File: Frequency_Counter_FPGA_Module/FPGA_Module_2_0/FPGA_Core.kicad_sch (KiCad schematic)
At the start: 97 parts, among them J1 Channel A, J2 Channel B, J3 CH A Test, J4 CH B Test, J5 GPS, J6 Input_board, J7 STM_mainboard, U1 MAX9601, U12 TLV9001IDCK, U2 MC100EP016A, U20 MC100EPT23DT, U24 MC100EPT23DT

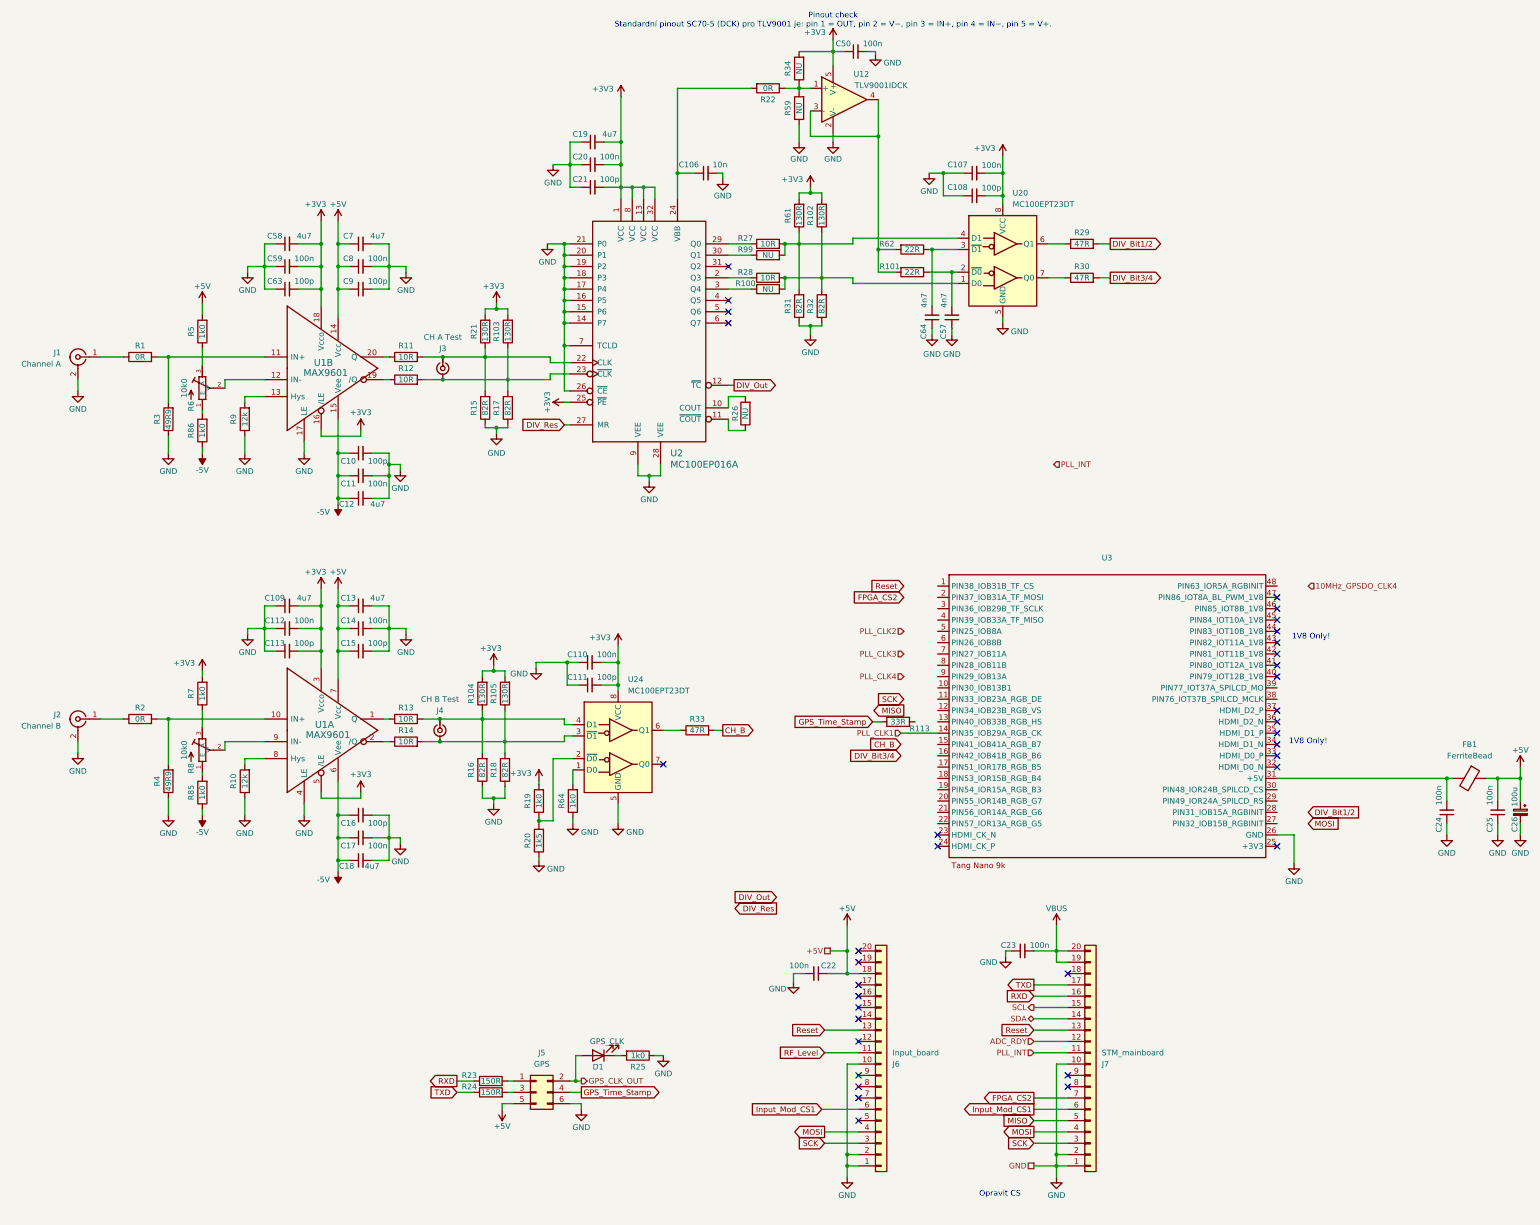
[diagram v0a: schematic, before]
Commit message: feat(boot): LED selftest blikaci kod + RTC LSE medium-low drive; UI 4.3" audit; FPGA HW revize
STM32H757 firmware:
- bootled.c/h: boot-time HW selftest diagnostika na LED_1 (PG3). Kazdy
  sledovany periferni init (FMC/SPI2/I2C4/DSIHOST/LTDC/USART1/RTC/ADC3/
  QUADSPI/I2C1) + display bring-up (panel probe/power-on/DSI start/
  TC358762) si zaznamena poradove cislo; pri zaseknuti v Error_Handler()
  LED bez displeje zabliká N-krat podle poradi. Regen-safe (jen chranene
  USER CODE hooky), bez zpozdeni v happy-path.
- RTC LSE Drive Capability LOW -> MEDIUM LOW (H757_LED.ioc): kompenzuje
  desky s predimenzovanymi zatezovymi kondenzatory krystalu (22pF misto
  18pF), ktere LSE nerozjizdely.
- UI audit pro realny 4,3" 800x480 panel (8,54 px/mm): hit-slop pilulek,
  fonty, HDR_PILL_LIMIT fit-check, Menu 3x4 mrizka s placeholdery, oprava
  ghost bugu AUTO CET/CEST tlacitka, sign-loss bug ve fmt_fixed/fmt_minmax.
  main-old layout zamrazen jako default (A/B srovnani, viz STATUS.md #14).

FPGA carrier v2.0 (KiCad): prubezne review checklisty a schema/PCB revize.

Co-Authored-By: OK2JNJ <ok2jnj@local>
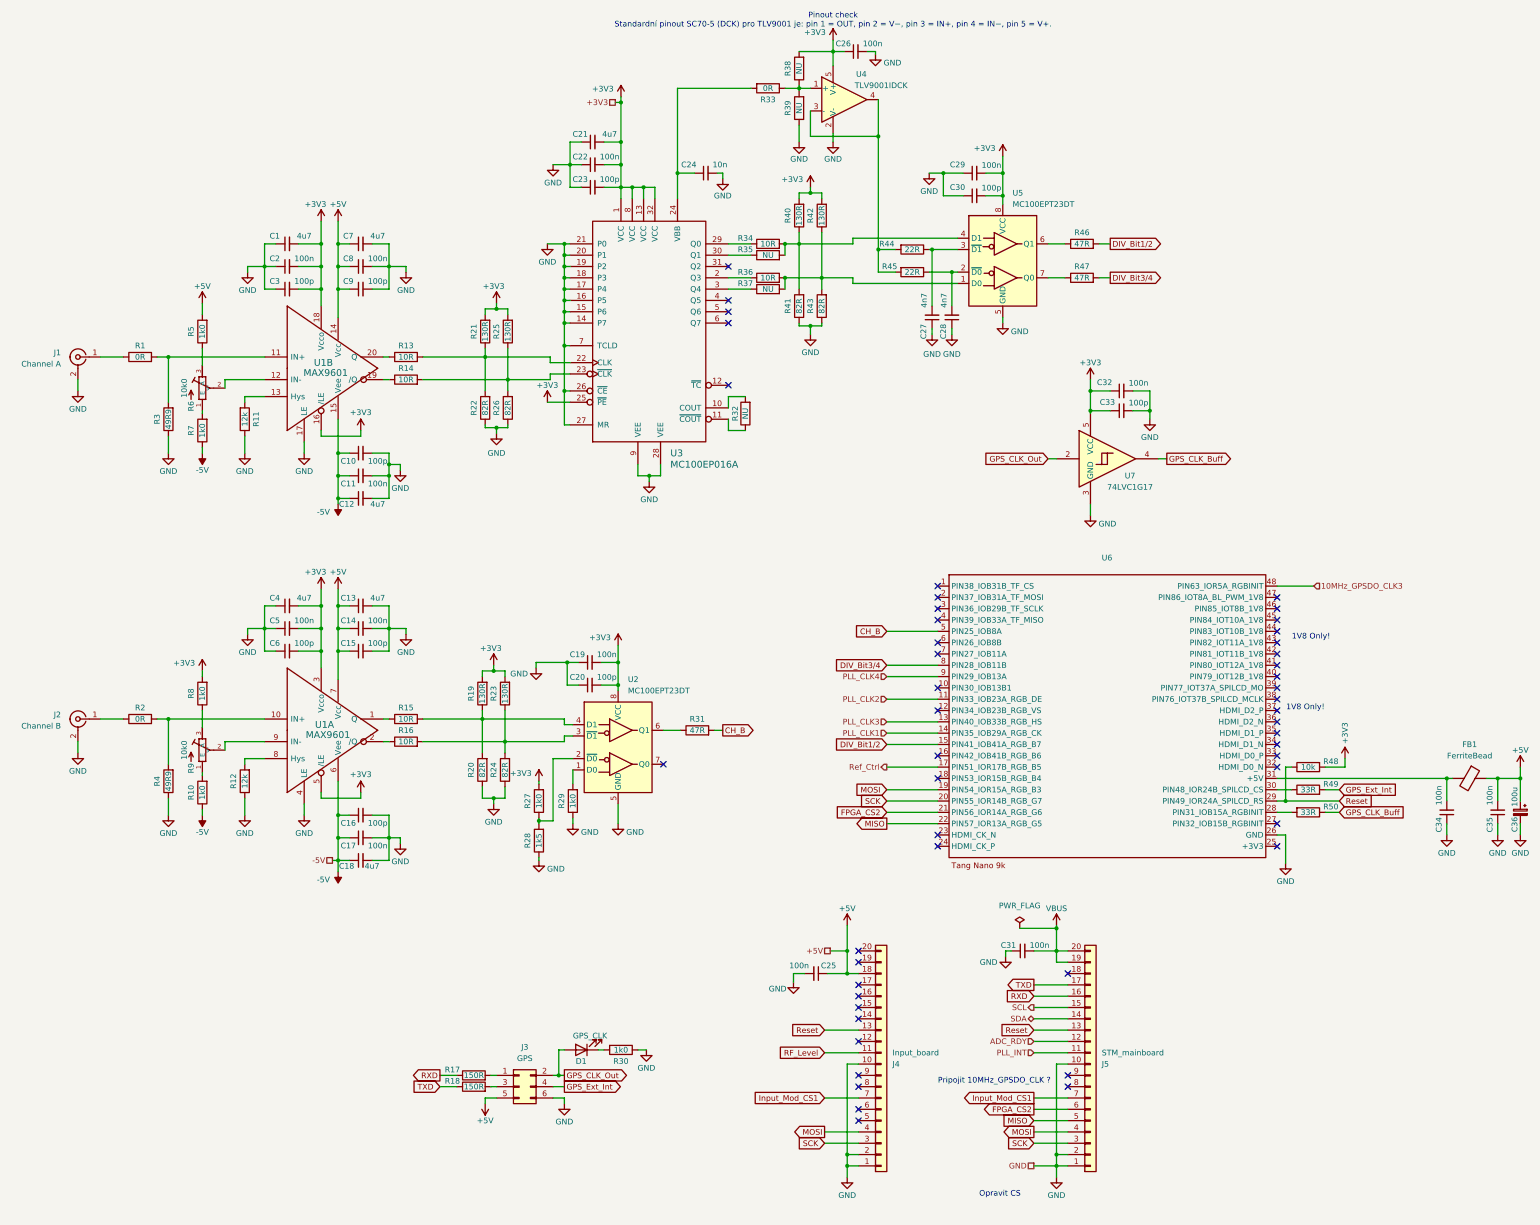
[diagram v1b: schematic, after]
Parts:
- removed J3: CH A Test, Connector_Coaxial:U.FL_Hirose_U.FL-R-SMT-1_Vertical, symbol Connector:Conn_Coaxial_Small
- removed J4: CH B Test, Connector_Coaxial:U.FL_Hirose_U.FL-R-SMT-1_Vertical, symbol Connector:Conn_Coaxial_Small
- removed U2: MC100EP016A, Package_QFP:LQFP-32_7x7mm_P0.8mm, symbol Counter_main-cache:MC100EP016A-RESCUE-Counter
- added C32: 100n, Capacitor_SMD:C_0805_2012Metric, symbol Device:C_Small
- added C33: 100p, Capacitor_SMD:C_0805_2012Metric, symbol Device:C_Small
- added R48: 10k, Resistor_SMD:R_0805_2012Metric, symbol Device:R
- added R50: 33R, Resistor_SMD:R_0805_2012Metric, symbol Device:R
- added U3: MC100EP016A, Package_QFP:LQFP-32_7x7mm_P0.8mm, symbol Counter_main-cache:MC100EP016A-RESCUE-Counter
- added U7: 74LVC1G17, Package_TO_SOT_SMD:SOT-23-5, symbol 74xGxx:74LVC1G17
- U6: renamed from U3; value ~ -> (none)
- renumbered C58 to C1, C110 to C19, C59 to C2, C111 to C20, C19 to C21, C20 to C22, C21 to C23, C106 to C24, C22 to C25, C50 to C26, C64 to C27, C57 to C28, C107 to C29, C63 to C3, C108 to C30, C23 to C31, C24 to C34, C25 to C35, C26 to C36, C109 to C4, C112 to C5, C113 to C6, J5 to J3, J6 to J4, J7 to J5, R85 to R10, R9 to R11, R10 to R12, R11 to R13, R12 to R14, R13 to R15, R14 to R16, R23 to R17, R24 to R18, R104 to R19, R16 to R20, R15 to R22, R105 to R23, R18 to R24, R103 to R25, R17 to R26, R19 to R27, R20 to R28, R64 to R29, R25 to R30, R33 to R31, R26 to R32, R22 to R33, R27 to R34, R99 to R35, R28 to R36, R100 to R37, R34 to R38, R59 to R39, R61 to R40, R31 to R41, R102 to R42, R32 to R43, R62 to R44, R101 to R45, R29 to R46, R30 to R47, R113 to R49, R86 to R7, R7 to R8, R8 to R9, U24 to U2, U12 to U4, U20 to U5
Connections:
- net +3V3: now also C32.1, C33.1, R48.2, U3.1 (VCC), U3.13 (VCC), U3.25 (~{PE}), U3.32 (VCC), U3.8 (VCC), U7.5 (VCC)
- net CH_B: now also U6.5 (PIN25_IOB8A)
- net DIV_Bit1/2: now also U6.15 (PIN41_IOB41A_RGB_B7)
- net DIV_Bit3/4: now also U6.8 (PIN28_IOB11B)
- net FPGA_CS2: now also J5.6 (Pin_6), U6.21 (PIN56_IOR14A_RGB_G6); no longer J5.7 (Pin_7)
- net GND: now also C32.2, C33.2, U3.14 (P7), U3.15 (P6), U3.16 (P5), U3.17 (P4), U3.18 (P3), U3.19 (P2), U3.20 (P1), U3.21 (P0), U3.26 (~{CE}), U3.27 (MR), U3.28 (VEE), U3.7 (TCLD), U3.9 (VEE), U7.3 (GND)
- net Input_Mod_CS1: now also J4.7 (Pin_7), J5.7 (Pin_7); no longer J4.6 (Pin_6), J5.6 (Pin_6)
- net MISO: now also U6.22 (PIN57_IOR13A_RGB_G5)
- net MOSI: now also U6.19 (PIN54_IOR15A_RGB_B3)
- net PLL_CLK2: now also U6.11 (PIN33_IOB23A_RGB_DE)
- net PLL_CLK3: now also U6.13 (PIN40_IOB33B_RGB_HS)
- net PLL_CLK4: now also U6.9 (PIN29_IOB13A)
- net Reset: now also U6.29 (PIN49_IOR24A_SPILCD_RS), R48.1
- net SCK: now also U6.20 (PIN55_IOR14B_RGB_G7)
- net at R37.1: now also U3.3 (Q4)
- net at R13.2, R21.1, R22.2: now also U3.22 (CLK)
- net at R14.2, R25.1, R26.2: now also U3.23 (~{CLK})
- net at C24.1, R33.2: now also U3.24 (VBB)
- net at R49.1: now also U6.30 (PIN48_IOR24B_SPILCD_CS)
- net at R36.1: now also U3.2 (Q3)
- net at R35.1: now also U3.30 (Q1)
- net at R32.1: now also U3.11 (~{COUT})
- net at R32.2: now also U3.10 (COUT)
- net at R34.1: now also U3.29 (Q0)
- net Ref_Ctrl: now reaches U6.17 (PIN51_IOR17B_RGB_B5)
- net at U6.28 (PIN31_IOB15A_RGBINIT): now also R50.2
- net 10MHz_GPSDO_CLK3: now reaches U6.48 (PIN63_IOR5A_RGBINIT)
- net GPS_CLK_OUT renamed GPS_CLK_Out
- net GPS_CLK_Out: now also U7.2
- net GPS_Time_Stamp renamed GPS_Ext_Int
- new net GPS_CLK_Buff: R50.1, U7.4
- no-connect marks 36 -> 50
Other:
- note added: "Pripojit 10MHz_GPSDO_CLK ?"
- moved on the sheet: D1, J3, R11, R17, R18, R30, R49

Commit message: feat(hw): FPGA carrier v2.0 — aktualizace schematu + PCB + checklist
KiCad FPGA_Module_2_0 (FPGA_Core/GPSDO/I2C_devices/power_supply schemata,
PCB layout, project), BOARD_V20_CHECKLIST.md. Odstranen zastaraly
FPGA_module_schematic.pdf (nahrazen exportem FPGA_module.pdf).

Co-Authored-By: OK2JNJ <ok2jnj@users.noreply.github.com>
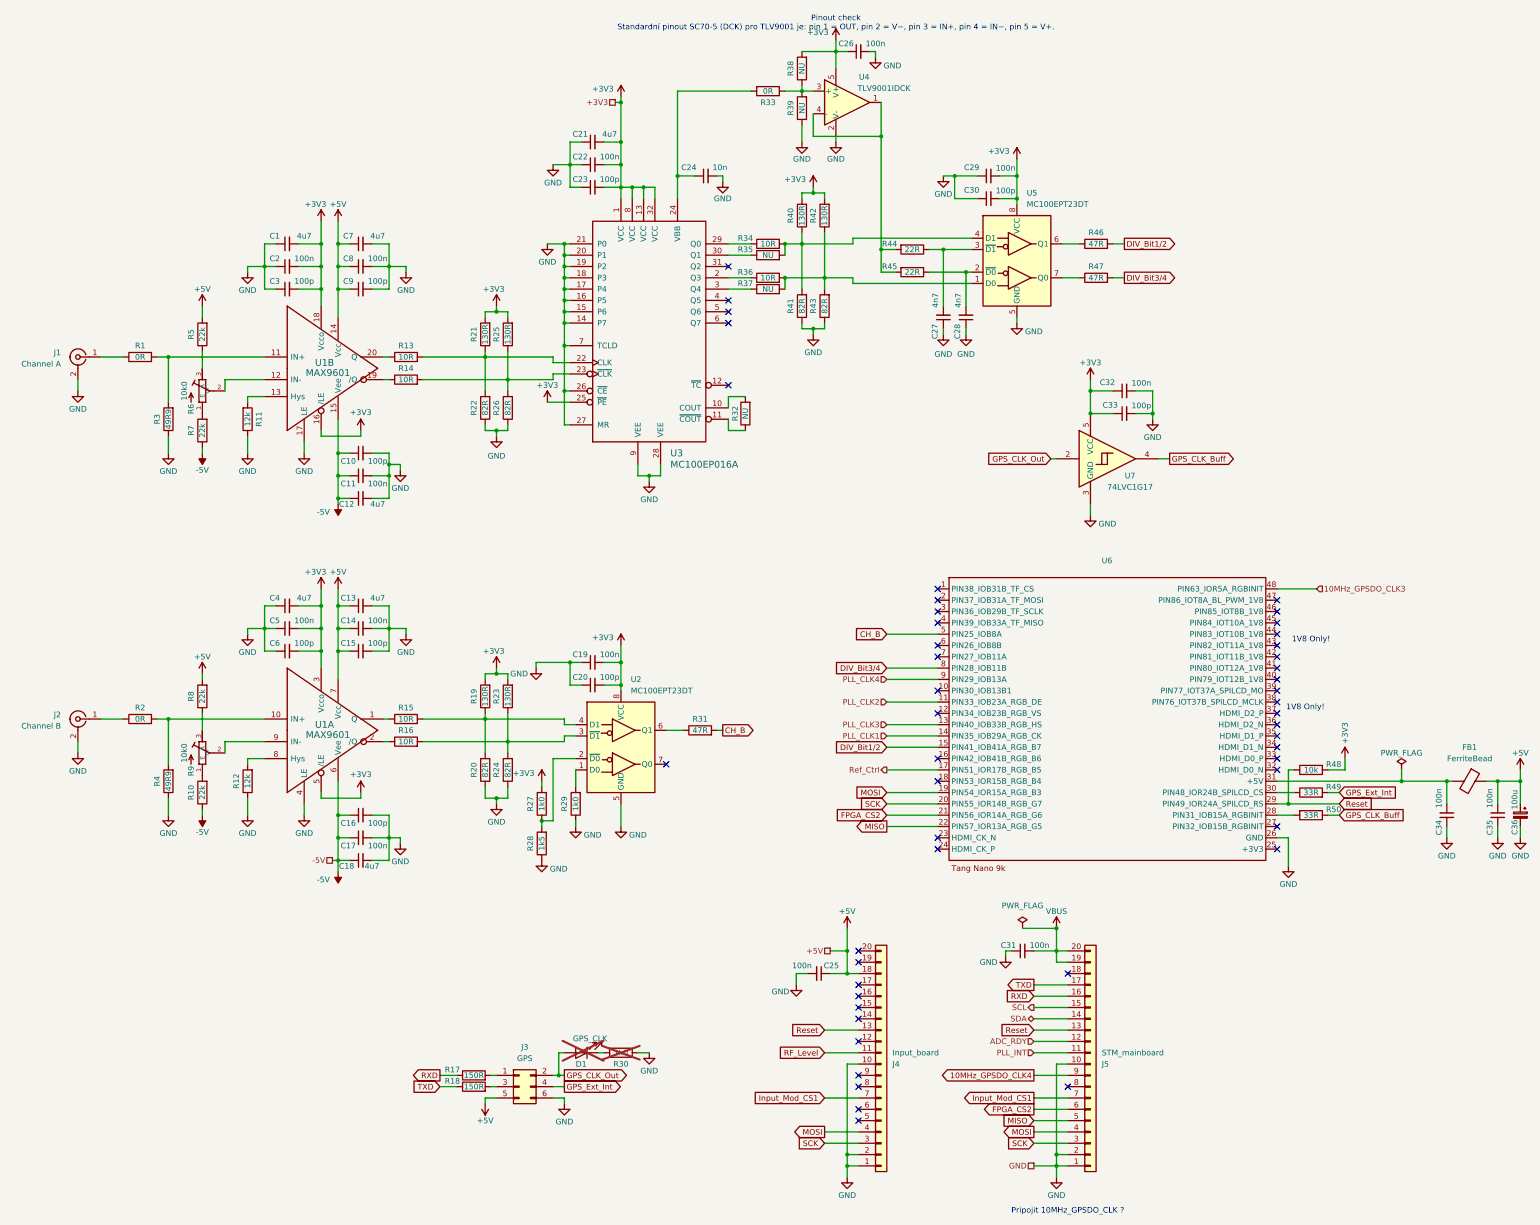
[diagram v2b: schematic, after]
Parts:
- D1, R30: now not fitted
- R10, R5, R7, R8: value 1k0 -> 22k; LCSC PN C17513 -> (none); LCSC link https://www.lcsc.com/product-detail/Chip-Resistor-Surface-M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 -> (none)
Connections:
- net +3V3: no longer R8.2
- net +5V: now also R8.2
- net at R33.1, R38.1, R39.2: now also U4.3 (+); no longer U4.1 (+)
- net at R44.2, R45.2, U4.4 (-): now also U4.1; no longer U4.3 (-)
- net 10MHz_GPSDO_CLK4: now reaches J5.9 (Pin_9)
- no-connect marks 50 -> 49
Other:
- note removed: "Opravit CS"
- moved on the sheet: C19, C20, C24, C25, C26, C27, C28, C29, C30, C32, C33, C34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
